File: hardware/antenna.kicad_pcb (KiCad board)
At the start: 2 copper layers, 9 parts, among them P1 CONN_01X05

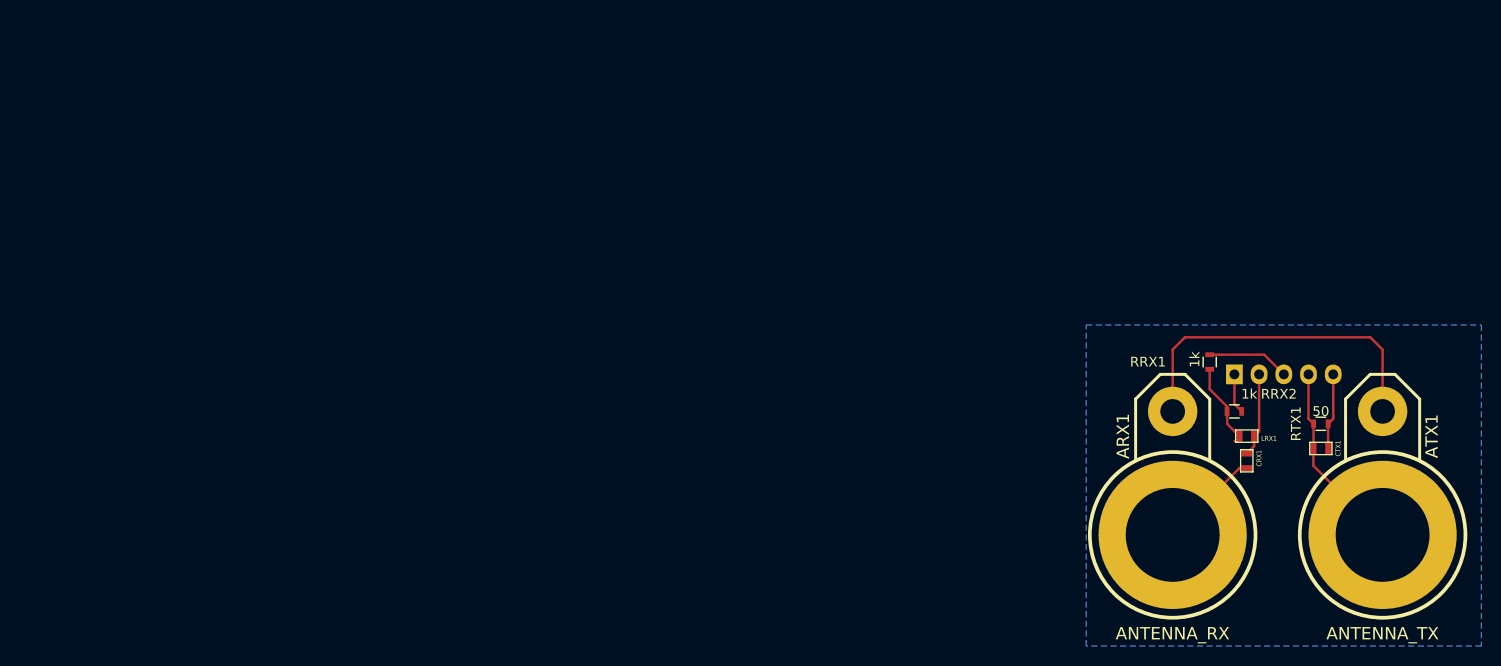
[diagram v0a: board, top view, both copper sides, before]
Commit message: Fixing up the antenna board.
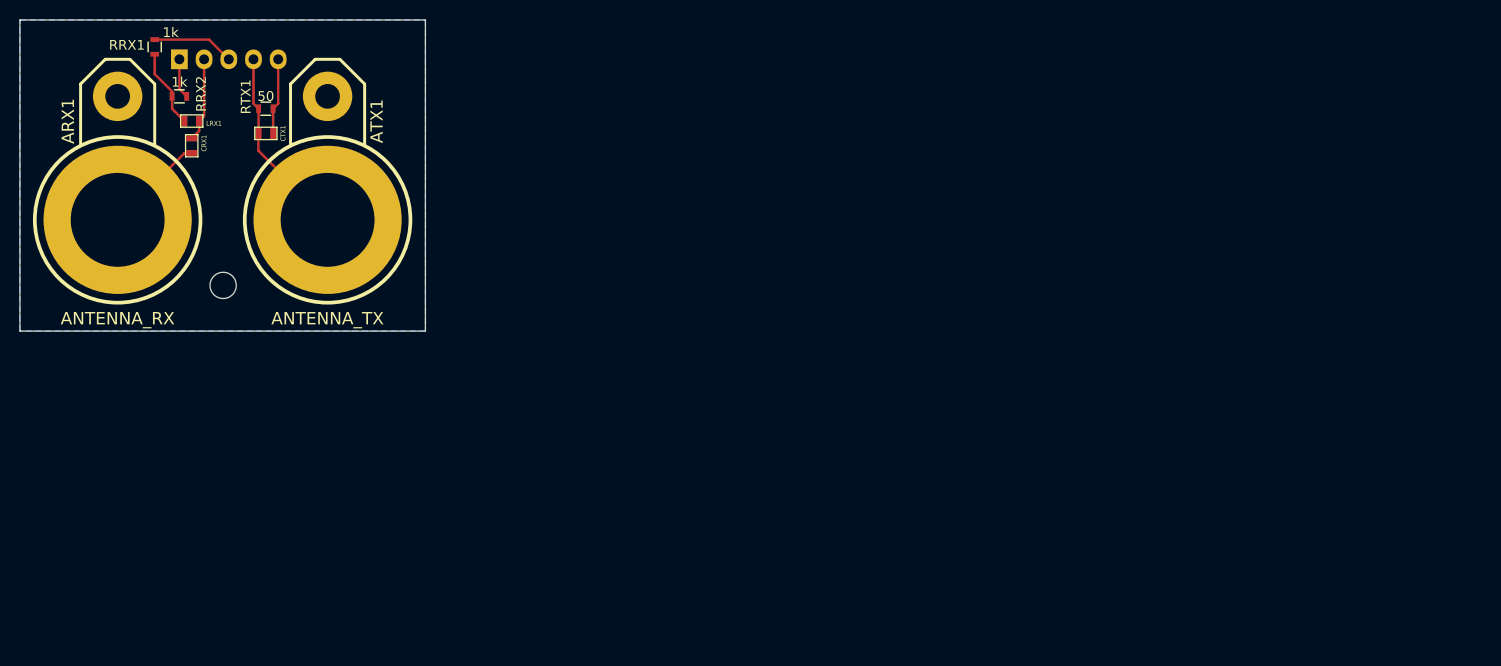
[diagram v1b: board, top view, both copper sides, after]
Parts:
- added MountingHole_2-7mm: VAL**, Mounting_Holes:MountingHole_2-7mm, F.Cu at (35.7, 41.6)
- moved ARX1 113.2 mm to (24.9, 34.9)
- moved ATX1 113.2 mm to (46.4, 34.9)
- moved CRX1 113.2 mm to (32.5, 27.3)
- moved CTX1 113.2 mm to (40.1, 26.0)
- moved LRX1 113.2 mm to (32.5, 24.8)
- moved P1 113.2 mm to (36.3, 18.4)
- moved RRX1 113.2 mm to (28.7, 17.1)
- moved RTX1 113.2 mm to (40.1, 23.5)
- moved RRX2 113.2 mm to (31.2, 22.2)
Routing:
- net AGND: track 47.3 -> 12.0 mm
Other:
- board outline added: 41.7 x 32 mm

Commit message: Small adjustments from doing paper fit.
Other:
- board text added: "G I V O G"
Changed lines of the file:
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@@
     (area 14.749999 14.299999 176.55 90.050001)
     (thickness 1.6)
-    (drawings 8)
+    (drawings 10)
     (tracks 26)
     (zones 0)
@@
   (layers
     (0 F.Cu signal)
-    (31 B.Cu signal)
+    (31 B.Cu signal hide)
     (32 B.Adhes user)
     (33 F.Adhes user)
@@
     (38 B.Mask user)
     (39 F.Mask user)
-    (40 Dwgs.User user hide)
+    (40 Dwgs.User user)
     (41 Cmts.User user)
     (42 Eco1.User user)
@@
     (descr "Through hole pin header")
     (tags "pin header")
-    (fp_text reference P1 (at 0 -2.286) (layer B.SilkS)
+    (fp_text reference P1 (at -0.43 2.3) (layer B.SilkS)
       (effects (font (size 1.27 1.27) (thickness 0.2032)) (justify mirror))
     )
@@
       (effects (font (size 1 1) (thickness 0.15)))
     )
-    (fp_text value 1k (at -1.48 -1.64 360) (layer F.SilkS)
+    (fp_text value 1k (at -1.58 1.86 360) (layer F.SilkS)
       (effects (font (size 1 1) (thickness 0.15)))
     )
@@
     (pad 1 thru_hole circle (at 0 0) (size 2.70002 2.70002) (drill 2.70002) (layers))
   )
+  (dimension 22.850055 (width 0.3) (layer Dwgs.User)
+    (gr_text "22.850 mm" (at 25.4 12.9 359.8746265) (layer Dwgs.User)
+      (effects (font (size 1.5 1.5) (thickness 0.3)))
+    )
+    (feature1 (pts (xy 37.65 14.35) (xy 37.65 14.35)))
+    (feature2 (pts (xy 14.8 14.3) (xy 14.8 14.3)))
+    (crossbar (pts (xy 14.8 14.3) (xy 37.65 14.35)))
+    (arrow1a (pts (xy 37.65 14.35) (xy 36.522216 14.933954)))
+    (arrow1b (pts (xy 37.65 14.35) (xy 36.524782 13.761116)))
+    (arrow2a (pts (xy 14.8 14.3) (xy 15.925218 14.888884)))
+    (arrow2b (pts (xy 14.8 14.3) (xy 15.927784 13.716046)))
+  )
+  (gr_text "G\nI\nV\nO\nG" (at 36.2 16 90) (layer F.SilkS)
+    (effects (font (size 1.6 1.5) (thickness 0.3)))
+  )
   (gr_line (start 14.8 46.35) (end 14.8 14.35) (angle 90) (layer Edge.Cuts) (width 0.1))
   (gr_line (start 56.5 46.35) (end 14.8 46.35) (angle 90) (layer Edge.Cuts) (width 0.1))
@@
     (arrow2b (pts (xy 154.95 83.05) (xy 156.076504 82.463579)))
   )
+  (segment (start 26.12 34.91) (end 26.12 31.862) (width 0.254) (layer F.Cu) (net 1))
+  (segment (start 31.708 28.052) (end 24.85 34.91) (width 0.254) (layer F.Cu) (net 1))
   (segment (start 32.47 28.052) (end 31.708 28.052) (width 0.254) (layer F.Cu) (net 1))
-  (segment (start 31.708 28.052) (end 24.85 34.91) (width 0.254) (layer F.Cu) (net 1))
-  (segment (start 26.12 34.91) (end 26.12 31.862) (width 0.254) (layer F.Cu) (net 1))
+  (segment (start 41.36 22.96) (end 40.84 23.48) (width 0.254) (layer F.Cu) (net 2))
+  (segment (start 41.36 18.4) (end 41.36 22.96) (width 0.254) (layer F.Cu) (net 2))
+  (segment (start 40.84 26.008) (end 40.852 26.02) (width 0.254) (layer F.Cu) (net 2))
+  (segment (start 40.84 23.48) (end 40.84 26.008) (width 0.254) (layer F.Cu) (net 2))
+  (segment (start 31.2 21.46) (end 31.95 22.21) (width 0.254) (layer F.Cu) (net 2))
   (segment (start 31.2 18.4) (end 31.2 21.46) (width 0.254) (layer F.Cu) (net 2))
-  (segment (start 31.2 21.46) (end 31.95 22.21) (width 0.254) (layer F.Cu) (net 2))
-  (segment (start 40.84 23.48) (end 40.84 26.008) (width 0.254) (layer F.Cu) (net 2))
-  (segment (start 40.84 26.008) (end 40.852 26.02) (width 0.254) (layer F.Cu) (net 2))
-  (segment (start 41.36 18.4) (end 41.36 22.96) (width 0.254) (layer F.Cu) (net 2))
-  (segment (start 41.36 22.96) (end 40.84 23.48) (width 0.254) (layer F.Cu) (net 2))
+  (segment (start 38.82 22.96) (end 39.34 23.48) (width 0.254) (layer F.Cu) (net 3))
+  (segment (start 38.82 18.4) (end 38.82 22.96) (width 0.254) (layer F.Cu) (net 3))
+  (segment (start 39.34 26.008) (end 39.328 26.02) (width 0.254) (layer F.Cu) (net 3))
+  (segment (start 39.34 23.48) (end 39.34 26.008) (width 0.254) (layer F.Cu) (net 3))
+  (segment (start 39.328 27.798) (end 46.44 34.91) (width 0.254) (layer F.Cu) (net 3))
   (segment (start 39.328 26.02) (end 39.328 27.798) (width 0.254) (layer F.Cu) (net 3))
-  (segment (start 39.328 27.798) (end 46.44 34.91) (width 0.254) (layer F.Cu) (net 3))
-  (segment (start 39.34 23.48) (end 39.34 26.008) (width 0.254) (layer F.Cu) (net 3))
-  (segment (start 39.34 26.008) (end 39.328 26.02) (width 0.254) (layer F.Cu) (net 3))
-  (segment (start 38.82 18.4) (end 38.82 22.96) (width 0.254) (layer F.Cu) (net 3))
-  (segment (start 38.82 22.96) (end 39.34 23.48) (width 0.254) (layer F.Cu) (net 3))
+  (segment (start 33.74 24.242) (end 33.232 24.75) (width 0.254) (layer F.Cu) (net 4))
+  (segment (start 33.74 18.4) (end 33.74 24.242) (width 0.254) (layer F.Cu) (net 4))
+  (segment (start 33.232 25.766) (end 32.47 26.528) (width 0.254) (layer F.Cu) (net 4))
   (segment (start 33.232 24.75) (end 33.232 25.766) (width 0.254) (layer F.Cu) (net 4))
-  (segment (start 33.232 25.766) (end 32.47 26.528) (width 0.254) (layer F.Cu) (net 4))
-  (segment (start 33.74 18.4) (end 33.74 24.242) (width 0.254) (layer F.Cu) (net 4))
-  (segment (start 33.74 24.242) (end 33.232 24.75) (width 0.254) (layer F.Cu) (net 4))
+  (segment (start 30.45 23.492) (end 31.708 24.75) (width 0.254) (layer F.Cu) (net 5))
+  (segment (start 30.45 22.21) (end 30.45 23.492) (width 0.254) (layer F.Cu) (net 5))
+  (segment (start 28.66 19.924) (end 30.45 21.714) (width 0.254) (layer F.Cu) (net 5))
+  (segment (start 30.45 21.714) (end 30.45 22.21) (width 0.254) (layer F.Cu) (net 5))
   (segment (start 28.66 17.88) (end 28.66 19.924) (width 0.254) (layer F.Cu) (net 5))
-  (segment (start 30.45 21.714) (end 30.45 22.21) (width 0.254) (layer F.Cu) (net 5))
-  (segment (start 28.66 19.924) (end 30.45 21.714) (width 0.254) (layer F.Cu) (net 5))
-  (segment (start 30.45 22.21) (end 30.45 23.492) (width 0.254) (layer F.Cu) (net 5))
-  (segment (start 30.45 23.492) (end 31.708 24.75) (width 0.254) (layer F.Cu) (net 5))
+  (segment (start 34.26 16.38) (end 36.28 18.4) (width 0.254) (layer F.Cu) (net 6))
   (segment (start 28.66 16.38) (end 34.26 16.38) (width 0.254) (layer F.Cu) (net 6))
-  (segment (start 34.26 16.38) (end 36.28 18.4) (width 0.254) (layer F.Cu) (net 6))
   (zone (net 2) (net_name AGND) (layer B.Cu) (hatch edge 0.508)
     (connect_pads (clearance 0.508))
